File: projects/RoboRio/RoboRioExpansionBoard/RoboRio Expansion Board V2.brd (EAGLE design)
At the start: 56.6 x 77.5 mm, 125 parts, among them J1 RRINTERFACE-FEMALE, J10 SPI_MISO, J11 SPI_MOSI, J12 I2C_SCL, J13 I2C_SDA, J14 UART_TX, J15 UART_RX, J16 LCD, J17 ADC1, J18 ADC2, J19 ADC3, J2 MICROSD-HINGED, J20 ADC4, J21 ADC5, J22 ADC6, J23 ADC7, J25 PWM0, J26 PWM1, J27 PWM2, J28 PWM3, J29 PWM4, J3 51387-0578, J30 PWM5, J31 PWM6, J32 PWM7, J33 PWM8, J34 PWM9, J35 AI0, J36 AI1, J37 AI2, J38 AI3, J39 AO0, J4 GPIO0, J40 AO1, J5 GPIO1, J6 GPIO2, J7 GPIO3, J8 SPI_CS, J9 SPI_CLK, Q1 NPN-SOT416, Q2 NPN-SOT416, Q3 NPN-SOT416, U1 P8X32A-Q44_P, U2 24LC256ST, U3 FT232RL, U4 TC54VN43, U5 TPS2115APWR, U6 REG1117, U7 ADC124S01, U8 ADC124S01, Y1 5MHz

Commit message: More routing
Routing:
- net PWREN_L: track 10.9 -> 20.0 mm, vias 1 -> 2
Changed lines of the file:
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@@
 <wire x1="49.156" y1="59.937" x2="49.777" y2="59.937" width="0.4064" layer="1"/>
 <via x="37.084" y="52.324" extent="1-16" drill="0.6" shape="square"/>
+<wire x1="37.084" y1="52.324" x2="37.1094" y2="52.2986" width="1.27" layer="1"/>
+<wire x1="37.1094" y1="52.2986" x2="37.1094" y2="50.1904" width="1.27" layer="1"/>
 <wire x1="43.95" y1="71.949" x2="43.6" y2="73.66" width="0" layer="19" extent="1-1"/>
 <wire x1="40.73" y1="74.69" x2="43.6" y2="73.66" width="0" layer="19" extent="1-1"/>
@@
 <wire x1="22.8475" y1="37.4925" x2="17.1475" y2="43.1925" width="0" layer="19" extent="1-1"/>
 <wire x1="28.5475" y1="42.3925" x2="22.8475" y2="37.4925" width="0" layer="19" extent="1-1"/>
-<wire x1="37.084" y1="52.324" x2="37.1094" y2="52.2986" width="1.27" layer="1"/>
-<wire x1="37.1094" y1="52.2986" x2="37.1094" y2="50.1904" width="1.27" layer="1"/>
 </signal>
 <signal name="N$8">
@@
 <wire x1="44.87" y1="43.942" x2="44.87" y2="46.228" width="0.2032" layer="1"/>
 <wire x1="44.87" y1="46.228" x2="44.704" y2="46.394" width="0.2032" layer="1"/>
-<wire x1="44.704" y1="46.394" x2="44.704" y2="51.982" width="0.2032" layer="1"/>
+<wire x1="44.704" y1="46.394" x2="44.704" y2="50.673" width="0.2032" layer="1"/>
 <via x="41.529" y="58.547" extent="1-16" drill="0.6" shape="square"/>
+<wire x1="44.704" y1="50.673" x2="44.704" y2="51.982" width="0.2032" layer="1"/>
 <wire x1="40.039" y1="59.875" x2="40.097" y2="59.817" width="0.2032" layer="1"/>
 <wire x1="40.097" y1="59.817" x2="40.005" y2="59.817" width="0.2032" layer="1"/>
@@
 <wire x1="40.005" y1="58.928" x2="40.386" y2="58.547" width="0.2032" layer="1"/>
 <wire x1="40.386" y1="58.547" x2="41.529" y2="58.547" width="0.2032" layer="1"/>
-<wire x1="44.704" y1="51.982" x2="41.529" y2="58.547" width="0" layer="19" extent="1-1"/>
+<via x="44.704" y="50.673" extent="1-16" drill="0.6" shape="square"/>
+<wire x1="41.529" y1="58.547" x2="42.672" y2="57.404" width="0.2032" layer="16"/>
+<wire x1="42.672" y1="57.404" x2="42.672" y2="56.134" width="0.2032" layer="16"/>
+<wire x1="42.672" y1="56.134" x2="44.704" y2="54.102" width="0.2032" layer="16"/>
+<wire x1="44.704" y1="54.102" x2="44.704" y2="50.673" width="0.2032" layer="16"/>
 </signal>
 <signal name="N$11">

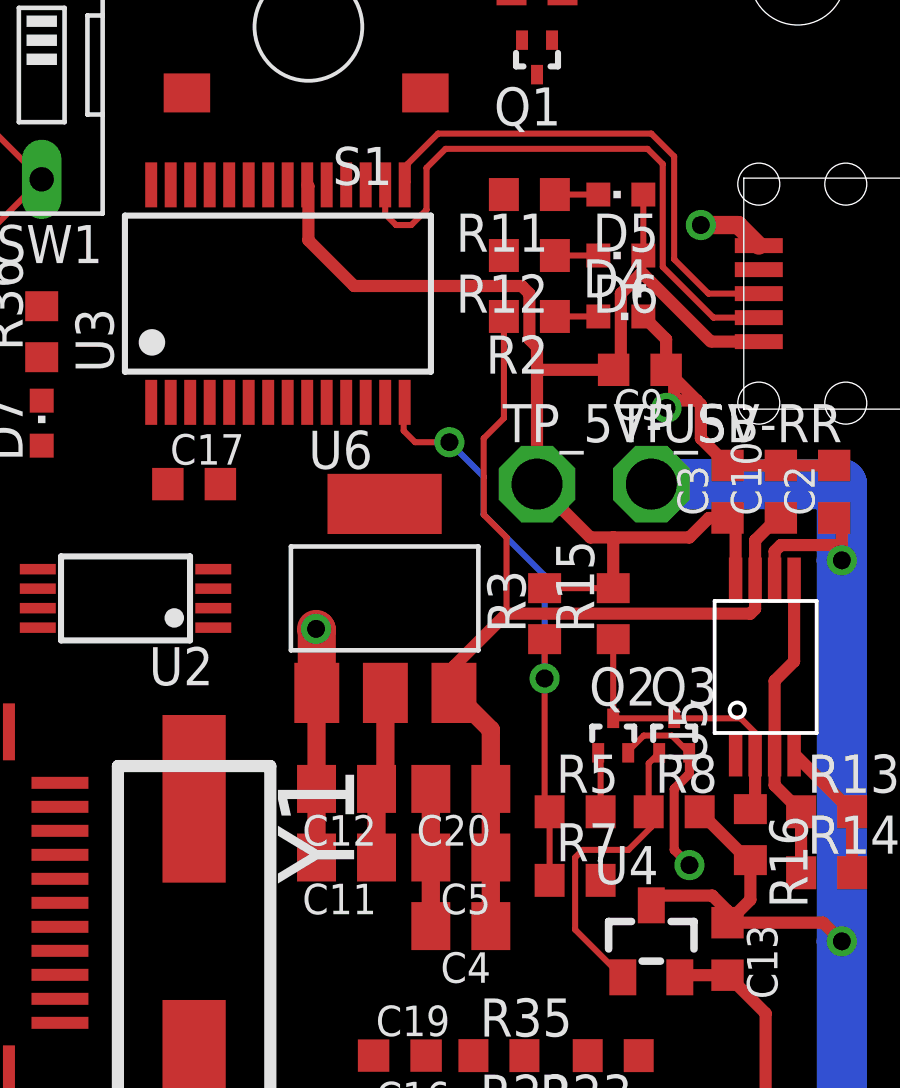
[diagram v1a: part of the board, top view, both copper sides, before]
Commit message: Adjusted 5VUSB so it doesn't cut off ground
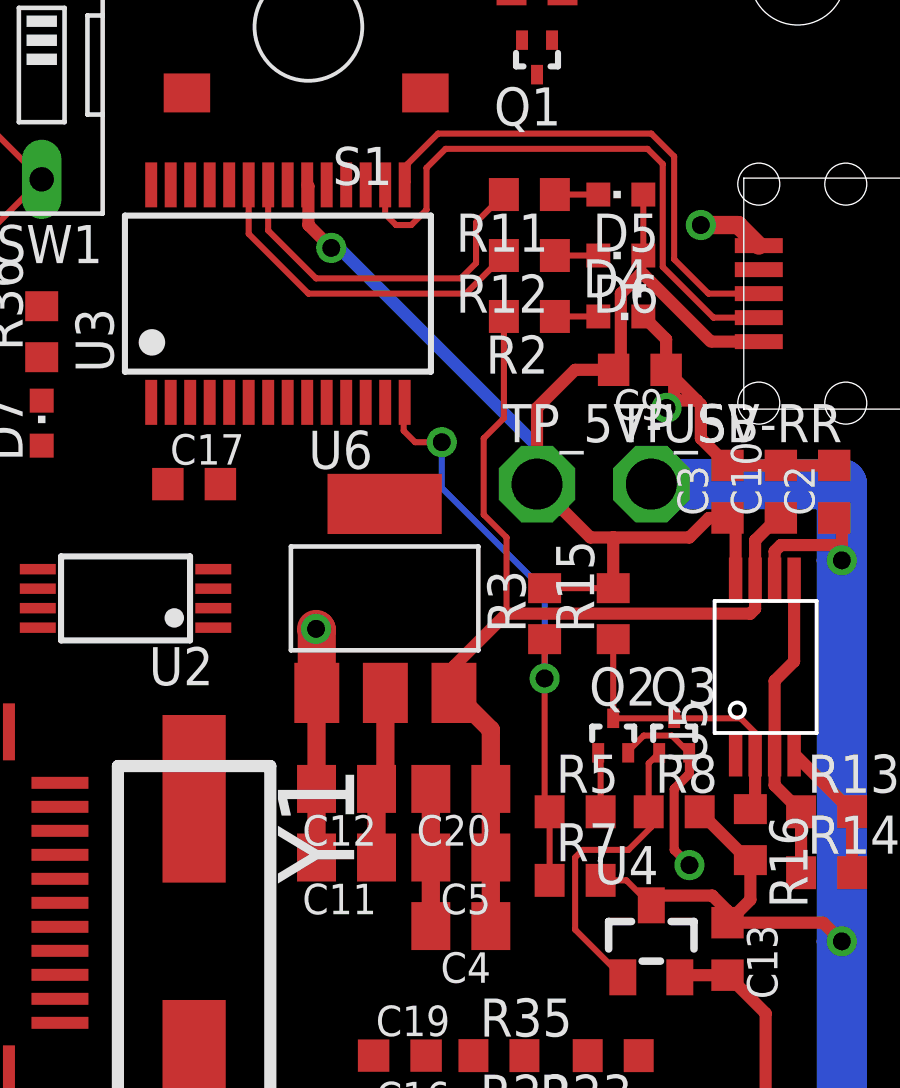
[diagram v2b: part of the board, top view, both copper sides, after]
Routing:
- net N$6: track 0.00 -> 12.0 mm
- net N$7: track 0.00 -> 11.5 mm
- net 5VRR: track 96.4 -> 98.5 mm
- net 5VUSB: track 44.6 -> 44.9 mm, vias 0 -> 1
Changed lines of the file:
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@@
 <layer number="29" name="tStop" color="7" fill="3" visible="yes" active="yes"/>
 <layer number="30" name="bStop" color="7" fill="6" visible="yes" active="yes"/>
-<layer number="31" name="tCream" color="7" fill="4" visible="yes" active="yes"/>
-<layer number="32" name="bCream" color="7" fill="5" visible="yes" active="yes"/>
-<layer number="33" name="tFinish" color="6" fill="3" visible="yes" active="yes"/>
-<layer number="34" name="bFinish" color="6" fill="6" visible="yes" active="yes"/>
-<layer number="35" name="tGlue" color="7" fill="4" visible="yes" active="yes"/>
-<layer number="36" name="bGlue" color="7" fill="5" visible="yes" active="yes"/>
+<layer number="31" name="tCream" color="7" fill="4" visible="no" active="yes"/>
+<layer number="32" name="bCream" color="7" fill="5" visible="no" active="yes"/>
+<layer number="33" name="tFinish" color="6" fill="3" visible="no" active="yes"/>
+<layer number="34" name="bFinish" color="6" fill="6" visible="no" active="yes"/>
+<layer number="35" name="tGlue" color="7" fill="4" visible="no" active="yes"/>
+<layer number="36" name="bGlue" color="7" fill="5" visible="no" active="yes"/>
 <layer number="37" name="tTest" color="7" fill="1" visible="yes" active="yes"/>
 <layer number="38" name="bTest" color="7" fill="1" visible="yes" active="yes"/>
@@
 <contactref element="D5" pad="A"/>
 <contactref element="D6" pad="A"/>
-<wire x1="44.196" y1="61.976" x2="44.196" y2="63.5" width="0.4064" layer="1"/>
-<wire x1="44.196" y1="63.5" x2="43.942" y2="63.754" width="0.4064" layer="1"/>
-<wire x1="43.942" y1="63.754" x2="38.354" y2="63.754" width="0.4064" layer="1"/>
-<wire x1="38.354" y1="63.754" x2="36.83" y2="65.278" width="0.4064" layer="1"/>
-<wire x1="36.83" y1="65.278" x2="36.83" y2="67.084" width="0.4064" layer="1"/>
 <wire x1="36.83" y1="67.084" x2="36.789" y2="67.125" width="0.4064" layer="1"/>
 <wire x1="47.994" y1="64.77" x2="47.994" y2="66.802" width="0.2032" layer="1"/>
@@
 <wire x1="47.994" y1="64.147" x2="50.241" y2="61.9" width="0.4064" layer="1"/>
 <wire x1="50.241" y1="61.9" x2="50.329" y2="61.9" width="0.2032" layer="1"/>
-<wire x1="44.196" y1="61.976" x2="44.45" y2="61.722" width="0.4064" layer="1"/>
-<wire x1="44.45" y1="61.722" x2="44.45" y2="60.96" width="0.4064" layer="1"/>
-<wire x1="44.45" y1="60.96" x2="44.45" y2="57.15" width="0.4064" layer="1"/>
-<wire x1="47.004" y1="60.96" x2="44.45" y2="60.96" width="0.4064" layer="1"/>
 <wire x1="47.004" y1="60.96" x2="47.244" y2="61.2" width="0.4064" layer="1"/>
 <wire x1="47.244" y1="61.2" x2="47.244" y2="63.5" width="0.4064" layer="1"/>
 <wire x1="47.244" y1="63.5" x2="47.891" y2="64.147" width="0.4064" layer="1"/>
 <wire x1="47.891" y1="64.147" x2="47.994" y2="64.147" width="0.4064" layer="1"/>
+<via x="37.592" y="65.024" extent="1-16" drill="0.6" shape="square"/>
+<wire x1="36.83" y1="67.084" x2="36.83" y2="65.786" width="0.4064" layer="1"/>
+<wire x1="36.83" y1="65.786" x2="37.592" y2="65.024" width="0.4064" layer="1"/>
+<wire x1="47.004" y1="60.96" x2="45.72" y2="60.96" width="0.4064" layer="1"/>
+<wire x1="45.72" y1="60.96" x2="44.45" y2="59.69" width="0.4064" layer="1"/>
+<wire x1="44.45" y1="59.69" x2="44.45" y2="57.15" width="0.4064" layer="1"/>
+<wire x1="37.592" y1="65.024" x2="37.592" y2="65.278" width="0.4064" layer="16"/>
+<wire x1="37.592" y1="65.278" x2="44.45" y2="58.42" width="0.4064" layer="16"/>
+<wire x1="44.45" y1="58.42" x2="44.45" y2="57.15" width="0.4064" layer="16"/>
 </signal>
 <signal name="N$4">
@@
 <wire x1="41.91" y1="12.7" x2="39.37" y2="12.7" width="1.27" layer="1"/>
 <wire x1="39.37" y1="12.7" x2="36.83" y2="12.7" width="1.27" layer="1"/>
-<wire x1="48.26" y1="43.11" x2="46.57" y2="43.942" width="0" layer="19" extent="1-1"/>
+<wire x1="48.26" y1="43.11" x2="47.428" y2="43.942" width="0.2032" layer="1"/>
+<wire x1="47.428" y1="43.942" x2="46.57" y2="43.942" width="0.2032" layer="1"/>
 <wire x1="31.75" y1="12.7" x2="36.83" y2="12.7" width="0" layer="19" extent="1-1"/>
 <wire x1="29.21" y1="12.7" x2="31.75" y2="12.7" width="0" layer="19" extent="1-1"/>
@@
 <wire x1="44.87" y1="46.228" x2="44.704" y2="46.394" width="0.2032" layer="1"/>
 <wire x1="44.704" y1="46.394" x2="44.704" y2="50.673" width="0.2032" layer="1"/>
-<via x="41.529" y="58.547" extent="1-16" drill="0.6" shape="square"/>
+<via x="41.275" y="58.547" extent="1-16" drill="0.6" shape="square"/>
 <wire x1="44.704" y1="50.673" x2="44.704" y2="51.982" width="0.2032" layer="1"/>
 <wire x1="40.039" y1="59.875" x2="40.097" y2="59.817" width="0.2032" layer="1"/>
@@
 <wire x1="40.005" y1="59.817" x2="40.005" y2="58.928" width="0.2032" layer="1"/>
 <wire x1="40.005" y1="58.928" x2="40.386" y2="58.547" width="0.2032" layer="1"/>
-<wire x1="40.386" y1="58.547" x2="41.529" y2="58.547" width="0.2032" layer="1"/>
+<wire x1="40.386" y1="58.547" x2="41.275" y2="58.547" width="0.2032" layer="1"/>
 <via x="44.704" y="50.673" extent="1-16" drill="0.6" shape="square"/>
-<wire x1="41.529" y1="58.547" x2="42.672" y2="57.404" width="0.2032" layer="16"/>
-<wire x1="42.672" y1="57.404" x2="42.672" y2="56.134" width="0.2032" layer="16"/>
-<wire x1="42.672" y1="56.134" x2="44.704" y2="54.102" width="0.2032" layer="16"/>
-<wire x1="44.704" y1="54.102" x2="44.704" y2="50.673" width="0.2032" layer="16"/>
+<wire x1="41.275" y1="58.547" x2="41.275" y2="57.023" width="0.2032" layer="16"/>
+<wire x1="41.275" y1="57.023" x2="44.704" y2="53.594" width="0.2032" layer="16"/>
+<wire x1="44.704" y1="53.594" x2="44.704" y2="50.673" width="0.2032" layer="16"/>
 </signal>
 <signal name="N$11">
@@
 <contactref element="R11" pad="2"/>
 <contactref element="U3" pad="22"/>
-<wire x1="35.489" y1="67.125" x2="43.346" y2="66.802" width="0" layer="19" extent="1-1"/>
+<wire x1="43.346" y1="66.802" x2="42.418" y2="65.874" width="0.2032" layer="1"/>
+<wire x1="42.418" y1="65.874" x2="42.418" y2="64.516" width="0.2032" layer="1"/>
+<wire x1="42.418" y1="64.516" x2="41.91" y2="64.008" width="0.2032" layer="1"/>
+<wire x1="41.91" y1="64.008" x2="37.084" y2="64.008" width="0.2032" layer="1"/>
+<wire x1="37.084" y1="64.008" x2="35.489" y2="65.603" width="0.2032" layer="1"/>
+<wire x1="35.489" y1="65.603" x2="35.489" y2="67.125" width="0.2032" layer="1"/>
 </signal>
 <signal name="N$7">
 <contactref element="R12" pad="2"/>
 <contactref element="U3" pad="23"/>
-<wire x1="34.839" y1="67.125" x2="43.346" y2="64.77" width="0" layer="19" extent="1-1"/>
+<wire x1="43.346" y1="64.77" x2="42.076" y2="63.5" width="0.2032" layer="1"/>
+<wire x1="42.076" y1="63.5" x2="36.83" y2="63.5" width="0.2032" layer="1"/>
+<wire x1="36.83" y1="63.5" x2="34.839" y2="65.491" width="0.2032" layer="1"/>
+<wire x1="34.839" y1="65.491" x2="34.839" y2="67.125" width="0.2032" layer="1"/>
 </signal>
 <signal name="N$18">
